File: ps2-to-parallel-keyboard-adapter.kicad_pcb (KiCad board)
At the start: 2 copper layers, 50.6 x 20.3 mm, 7 parts, among them J1 PS/2 Keyboard Mini DIN 6, J2 Ferguson Keyboard Connector J2, U1 PIC16F84A, Y1 4 MHz

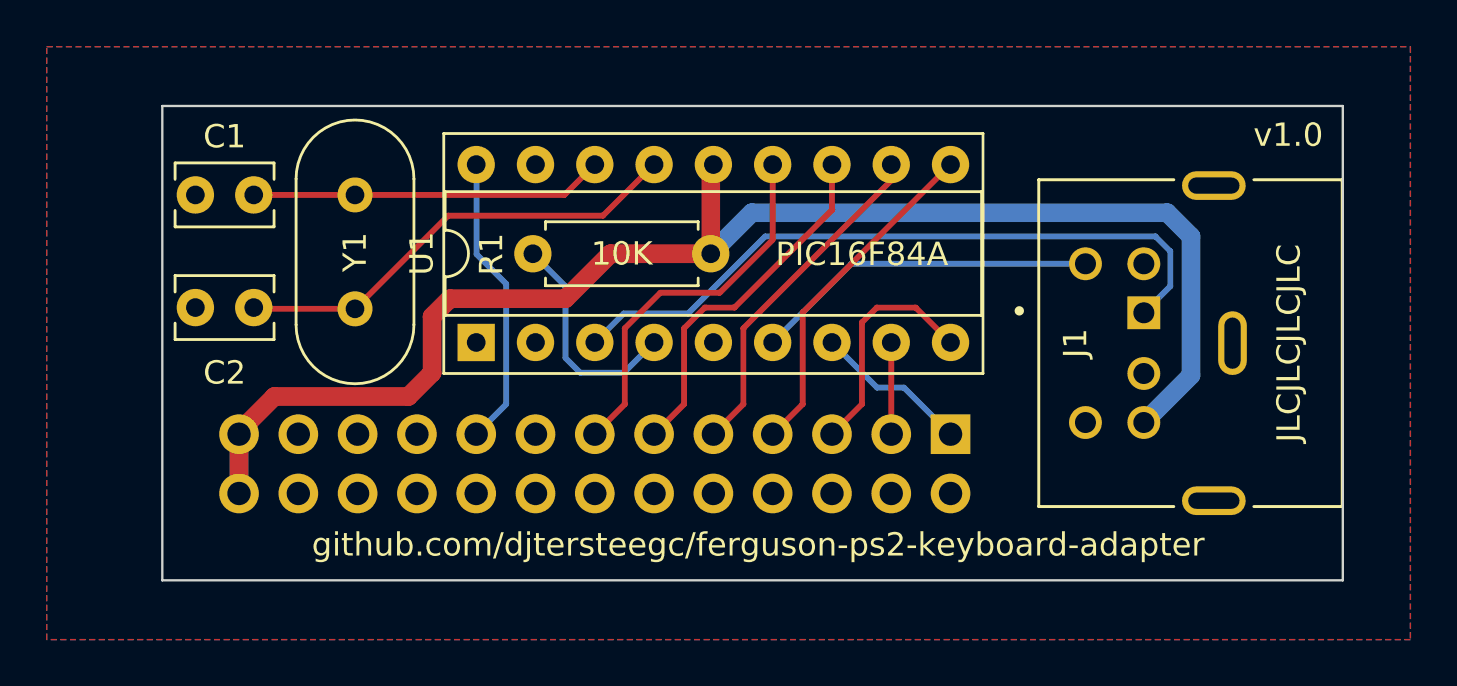
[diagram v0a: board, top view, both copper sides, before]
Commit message: v1.1, add decoupling cap
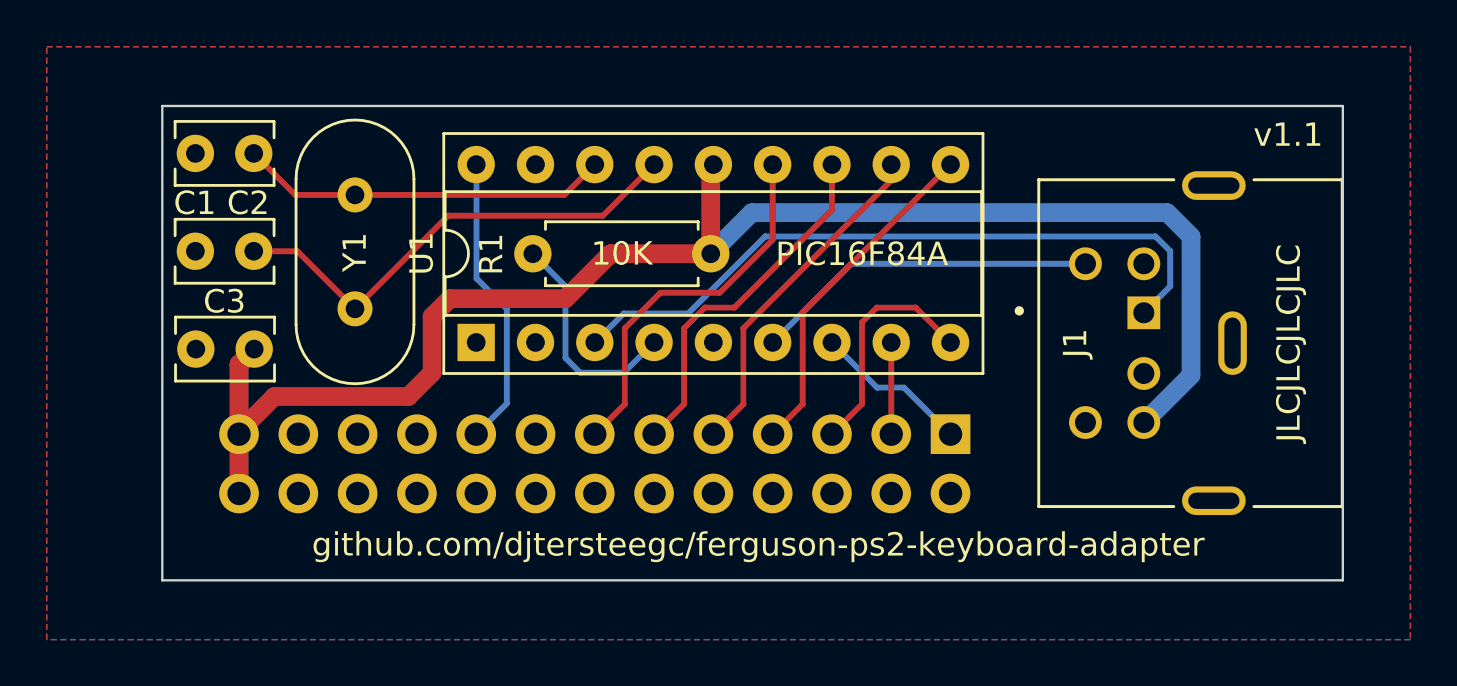
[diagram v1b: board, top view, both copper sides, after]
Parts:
- added C3: 0.1uf, Capacitor_THT:C_Rect_L4.0mm_W2.5mm_P2.50mm, F.Cu at (146.1, 104.4)
- C1, C2: value 10pf -> 22pf
- moved C2 2.41 mm to (143.5, 100.2)
- moved C1 1.78 mm to (143.5, 96.0)
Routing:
- net +5V: track 64.4 -> 72.2 mm
- net Net-(C2-Pad2): track 19.7 -> 20.7 mm
- net Net-(C1-Pad2): track 15.1 -> 15.9 mm
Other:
- board text added: "v1.1"
- board text removed: "v1.0"
